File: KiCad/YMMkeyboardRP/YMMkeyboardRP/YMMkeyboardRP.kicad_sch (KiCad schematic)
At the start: 53 parts, among them J2 Conn_01x02, J3 Conn_02x18_Odd_Even, J4 Conn_02x18_Odd_Even, J6 USB_B_Micro, J7 USB_C_Receptacle_USB2.0_16P, U1 XC6206PxxxMR, U2 W25Q32JVS, U3 RP2040, U5 NCP1117-3.3_SOT223, U7 NCP1117-3.3_SOT223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

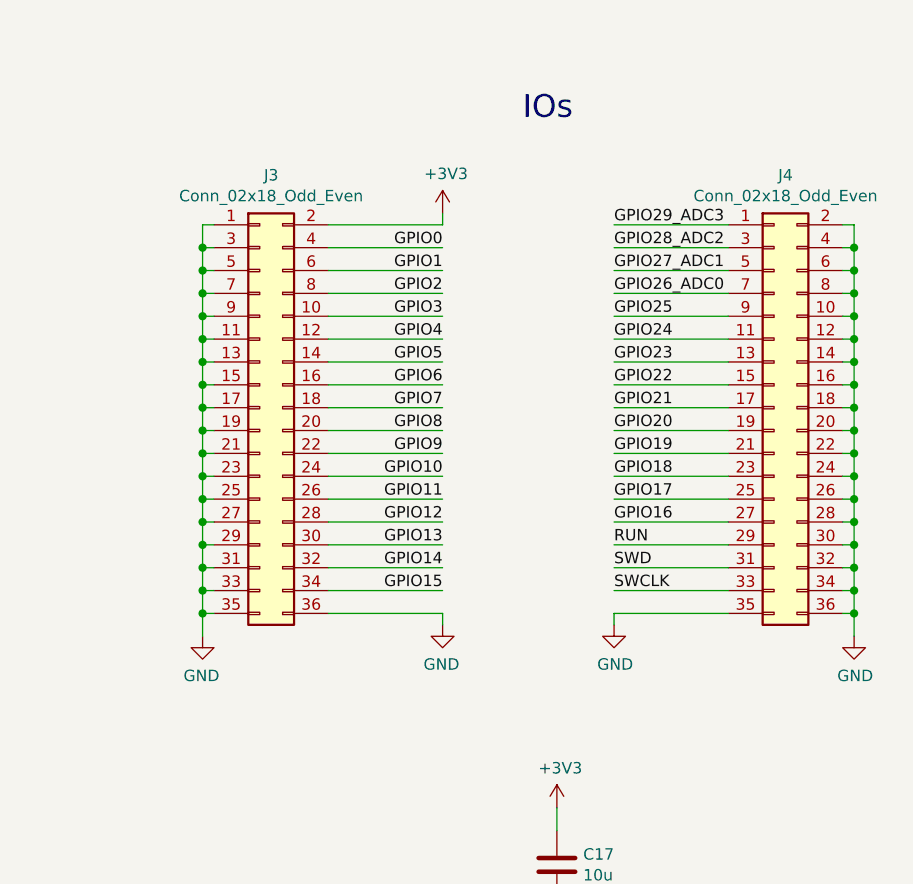
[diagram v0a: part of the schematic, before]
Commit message: rp2040の独自実装を検討
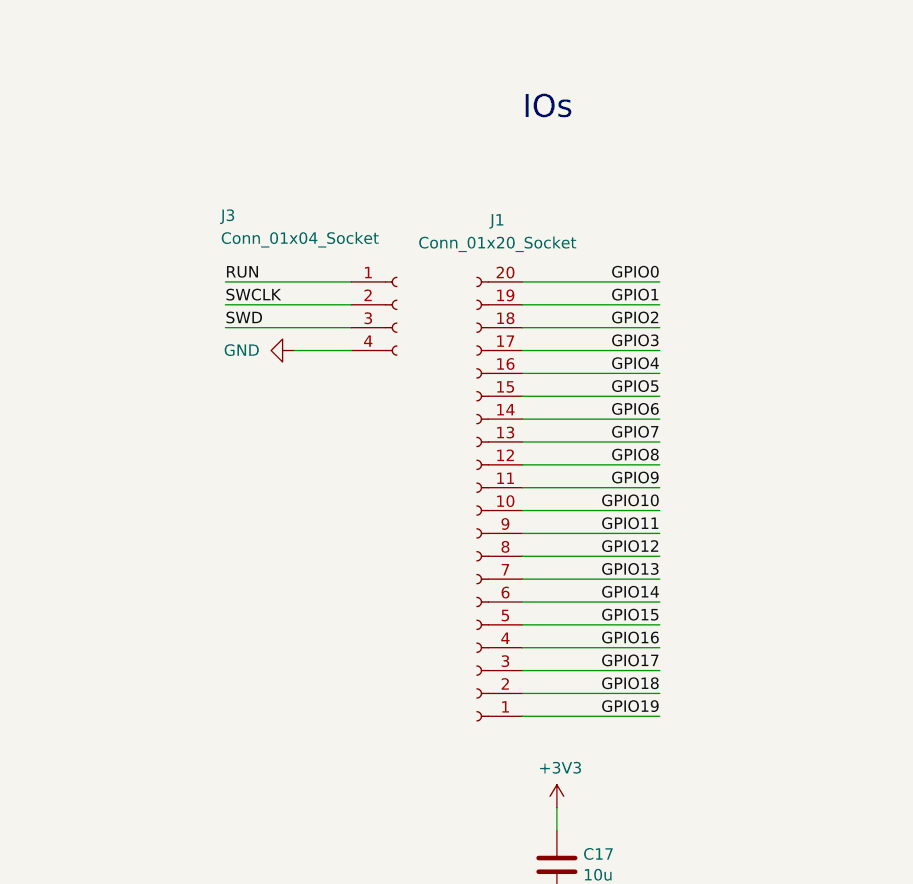
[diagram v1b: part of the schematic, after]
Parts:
- removed J3, J4: Conn_02x18_Odd_Even, Connector_PinHeader_2.54mm:PinHeader_2x18_P2.54mm_Vertical, symbol Connector_Generic:Conn_02x18_Odd_Even
- added J1: Conn_01x20_Socket, Connector_PinHeader_2.54mm:PinHeader_1x20_P2.54mm_Vertical, symbol Connector:Conn_01x20_Socket
- added J3: Conn_01x04_Socket, Connector_PinHeader_2.54mm:PinHeader_1x04_P2.54mm_Vertical, symbol Connector:Conn_01x04_Socket
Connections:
- net GND: now also J3.4 (Pin_4)
- net GPIO0: now also J1.20 (Pin_20)
- net GPIO1: now also J1.19 (Pin_19)
- net GPIO10: now also J1.10 (Pin_10)
- net GPIO11: now also J1.9 (Pin_9)
- net GPIO12: now also J1.8 (Pin_8)
- net GPIO13: now also J1.7 (Pin_7)
- net GPIO14: now also J1.6 (Pin_6)
- net GPIO15: now also J1.5 (Pin_5)
- net GPIO16: now also J1.4 (Pin_4)
- net GPIO17: now also J1.3 (Pin_3)
- net GPIO18: now also J1.2 (Pin_2)
- net GPIO19: now also J1.1 (Pin_1)
- net GPIO2: now also J1.18 (Pin_18)
- net GPIO3: now also J1.17 (Pin_17)
- net GPIO4: now also J1.16 (Pin_16)
- net GPIO5: now also J1.15 (Pin_15)
- net GPIO6: now also J1.14 (Pin_14)
- net GPIO7: now also J1.13 (Pin_13)
- net GPIO8: now also J1.12 (Pin_12)
- net GPIO9: now also J1.11 (Pin_11)
- net RUN: now also J3.1 (Pin_1)
- net SWCLK: now also J3.2 (Pin_2)
- net SWD: now also J3.3 (Pin_3)
